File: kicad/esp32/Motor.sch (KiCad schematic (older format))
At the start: 4 parts, among them P2 Motor_L, P3 Motor_R, U4 DRV8835

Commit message: 自動配線成功
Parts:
- renumbered C15 to C10, P2 to P1, P3 to P2
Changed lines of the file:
@@
 $Descr A4 11693 8268
 encoding utf-8
-Sheet 2 13
+Sheet 2 14
 Title ""
 Date ""
@@
 	5600 3100 5600 3200
 $Comp
-L GND #PWR016
+L GND #PWR013
 U 1 1 57CA1E38
 P 5400 4200
-F 0 "#PWR016" H 5400 3950 50  0001 C CNN
+F 0 "#PWR013" H 5400 3950 50  0001 C CNN
 F 1 "GND" H 5400 4050 50  0000 C CNN
 F 2 "" H 5400 4200 50  0000 C CNN
@@
 	5400 4200 5400 4100
 $Comp
-L GND #PWR017
+L GND #PWR014
 U 1 1 57CA1E3F
 P 5700 4200
-F 0 "#PWR017" H 5700 3950 50  0001 C CNN
+F 0 "#PWR014" H 5700 3950 50  0001 C CNN
 F 1 "GND" H 5700 4050 50  0000 C CNN
 F 2 "" H 5700 4200 50  0000 C CNN
@@
 	5700 4200 5700 4100
 $Comp
-L GND #PWR018
+L GND #PWR015
 U 1 1 57CA1E46
 P 4800 4200
-F 0 "#PWR018" H 4800 3950 50  0001 C CNN
+F 0 "#PWR015" H 4800 3950 50  0001 C CNN
 F 1 "GND" H 4800 4050 50  0000 C CNN
 F 2 "" H 4800 4200 50  0000 C CNN
@@
 Motor
 $Comp
-L C C15
+L C C10
 U 1 1 57CCEFE0
 P 4000 3650
-F 0 "C15" H 4025 3750 50  0000 L CNN
+F 0 "C10" H 4025 3750 50  0000 L CNN
 F 1 "0.1u" H 4025 3550 50  0000 L CNN
 F 2 "Capacitors_SMD:C_0201" H 4038 3500 50  0001 C CNN
@@
 $EndComp
 $Comp
-L GND #PWR019
+L GND #PWR016
 U 1 1 57CCF046
 P 4000 4200
-F 0 "#PWR019" H 4000 3950 50  0001 C CNN
+F 0 "#PWR016" H 4000 3950 50  0001 C CNN
 F 1 "GND" H 4000 4050 50  0000 C CNN
 F 2 "" H 4000 4200 50  0000 C CNN
@@
 	4000 3800 4000 4200
 $Comp
-L +BATT #PWR020
+L +BATT #PWR017
 U 1 1 57CD5BEE
 P 5600 3100
-F 0 "#PWR020" H 5600 2950 50  0001 C CNN
+F 0 "#PWR017" H 5600 2950 50  0001 C CNN
 F 1 "+BATT" H 5600 3240 50  0000 C CNN
 F 2 "" H 5600 3100 50  0000 C CNN
@@
 	4900 3700 4800 3700
 $Comp
-L CONN_01X02 P2
+L CONN_01X02 P1
 U 1 1 589D679E
 P 7700 3450
-F 0 "P2" H 7700 3600 50  0000 C CNN
+F 0 "P1" H 7700 3600 50  0000 C CNN
 F 1 "Motor_L" V 7800 3450 50  0000 C CNN
 F 2 "mouse:SMD_conn_2" H 7700 3450 50  0001 C CNN
@@
 $EndComp
 $Comp
-L CONN_01X02 P3
+L CONN_01X02 P2
 U 1 1 589D680E
 P 7700 3950
-F 0 "P3" H 7700 4100 50  0000 C CNN
+F 0 "P2" H 7700 4100 50  0000 C CNN
 F 1 "Motor_R" V 7800 3950 50  0000 C CNN
 F 2 "mouse:SMD_conn_2" H 7700 3950 50  0001 C CNN
@@
 	7500 3500 7400 3500
 $Comp
-L +3.3V #PWR021
+L +3.3V #PWR018
 U 1 1 589CC6A5
 P 5300 3100
-F 0 "#PWR021" H 5300 2950 50  0001 C CNN
+F 0 "#PWR018" H 5300 2950 50  0001 C CNN
 F 1 "+3.3V" H 5300 3240 50  0000 C CNN
 F 2 "" H 5300 3100 50  0000 C CNN
@@
 $EndComp
 $Comp
-L +3.3V #PWR022
+L +3.3V #PWR019
 U 1 1 589CC6C6
 P 4000 3100
-F 0 "#PWR022" H 4000 2950 50  0001 C CNN
+F 0 "#PWR019" H 4000 2950 50  0001 C CNN
 F 1 "+3.3V" H 4000 3240 50  0000 C CNN
 F 2 "" H 4000 3100 50  0000 C CNN

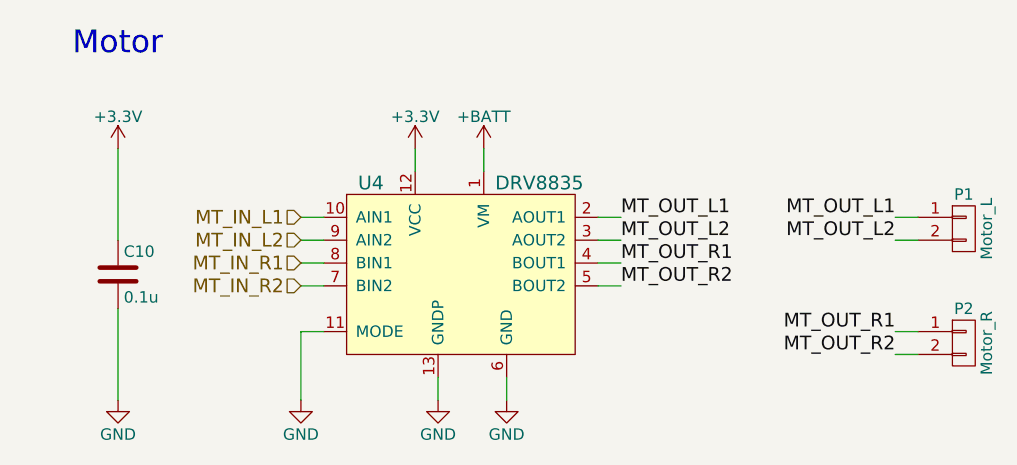
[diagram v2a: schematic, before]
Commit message: 2輪の基板を作成
部品を配置
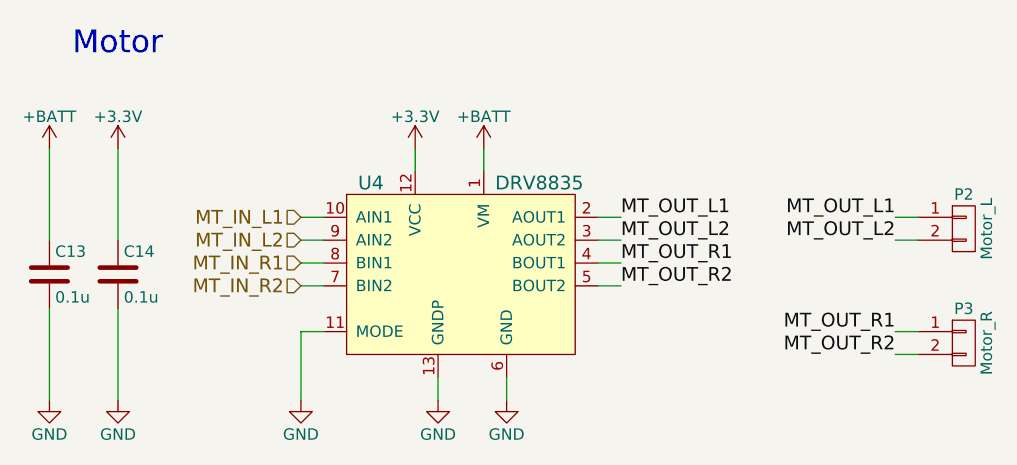
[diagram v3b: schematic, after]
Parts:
- added C13: 0.1u, Capacitors_SMD:C_0201, symbol C
- renumbered C10 to C14, P1 to P2, P2 to P3
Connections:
- net +BATT: now also C13.1
- net GND: now also C13.2
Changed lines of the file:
@@
 $Descr A4 11693 8268
 encoding utf-8
-Sheet 2 14
+Sheet 2 13
 Title ""
 Date ""
@@
 	5600 3100 5600 3200
 $Comp
-L GND #PWR013
+L GND #PWR014
 U 1 1 57CA1E38
 P 5400 4200
-F 0 "#PWR013" H 5400 3950 50  0001 C CNN
+F 0 "#PWR014" H 5400 3950 50  0001 C CNN
 F 1 "GND" H 5400 4050 50  0000 C CNN
 F 2 "" H 5400 4200 50  0000 C CNN
@@
 	5400 4200 5400 4100
 $Comp
-L GND #PWR014
+L GND #PWR015
 U 1 1 57CA1E3F
 P 5700 4200
-F 0 "#PWR014" H 5700 3950 50  0001 C CNN
+F 0 "#PWR015" H 5700 3950 50  0001 C CNN
 F 1 "GND" H 5700 4050 50  0000 C CNN
 F 2 "" H 5700 4200 50  0000 C CNN
@@
 	5700 4200 5700 4100
 $Comp
-L GND #PWR015
+L GND #PWR016
 U 1 1 57CA1E46
 P 4800 4200
-F 0 "#PWR015" H 4800 3950 50  0001 C CNN
+F 0 "#PWR016" H 4800 3950 50  0001 C CNN
 F 1 "GND" H 4800 4050 50  0000 C CNN
 F 2 "" H 4800 4200 50  0000 C CNN
@@
 Motor
 $Comp
-L C C10
+L C C14
 U 1 1 57CCEFE0
 P 4000 3650
-F 0 "C10" H 4025 3750 50  0000 L CNN
+F 0 "C14" H 4025 3750 50  0000 L CNN
 F 1 "0.1u" H 4025 3550 50  0000 L CNN
 F 2 "Capacitors_SMD:C_0201" H 4038 3500 50  0001 C CNN
@@
 $EndComp
 $Comp
-L GND #PWR016
+L GND #PWR017
 U 1 1 57CCF046
 P 4000 4200
-F 0 "#PWR016" H 4000 3950 50  0001 C CNN
+F 0 "#PWR017" H 4000 3950 50  0001 C CNN
 F 1 "GND" H 4000 4050 50  0000 C CNN
 F 2 "" H 4000 4200 50  0000 C CNN
@@
 	4000 3800 4000 4200
 $Comp
-L +BATT #PWR017
+L +BATT #PWR018
 U 1 1 57CD5BEE
 P 5600 3100
-F 0 "#PWR017" H 5600 2950 50  0001 C CNN
+F 0 "#PWR018" H 5600 2950 50  0001 C CNN
 F 1 "+BATT" H 5600 3240 50  0000 C CNN
 F 2 "" H 5600 3100 50  0000 C CNN
@@
 	4900 3700 4800 3700
 $Comp
-L CONN_01X02 P1
+L CONN_01X02 P2
 U 1 1 589D679E
 P 7700 3450
-F 0 "P1" H 7700 3600 50  0000 C CNN
+F 0 "P2" H 7700 3600 50  0000 C CNN
 F 1 "Motor_L" V 7800 3450 50  0000 C CNN
 F 2 "mouse:SMD_conn_2" H 7700 3450 50  0001 C CNN
@@
 $EndComp
 $Comp
-L CONN_01X02 P2
+L CONN_01X02 P3
 U 1 1 589D680E
 P 7700 3950
-F 0 "P2" H 7700 4100 50  0000 C CNN
+F 0 "P3" H 7700 4100 50  0000 C CNN
 F 1 "Motor_R" V 7800 3950 50  0000 C CNN
 F 2 "mouse:SMD_conn_2" H 7700 3950 50  0001 C CNN
@@
 	7500 3500 7400 3500
 $Comp
-L +3.3V #PWR018
+L +3.3V #PWR019
 U 1 1 589CC6A5
 P 5300 3100
-F 0 "#PWR018" H 5300 2950 50  0001 C CNN
+F 0 "#PWR019" H 5300 2950 50  0001 C CNN
 F 1 "+3.3V" H 5300 3240 50  0000 C CNN
 F 2 "" H 5300 3100 50  0000 C CNN
@@
 $EndComp
 $Comp
-L +3.3V #PWR019
+L +3.3V #PWR020
 U 1 1 589CC6C6
 P 4000 3100
-F 0 "#PWR019" H 4000 2950 50  0001 C CNN
+F 0 "#PWR020" H 4000 2950 50  0001 C CNN
 F 1 "+3.3V" H 4000 3240 50  0000 C CNN
 F 2 "" H 4000 3100 50  0000 C CNN
@@
 	1    0    0    -1
 $EndComp
+$Comp
+L +BATT #PWR021
+U 1 1 594721DF
+P 3700 3100
+F 0 "#PWR021" H 3700 2950 50  0001 C CNN
+F 1 "+BATT" H 3700 3240 50  0000 C CNN
+F 2 "" H 3700 3100 50  0000 C CNN
+F 3 "" H 3700 3100 50  0000 C CNN
+	1    3700 3100
+	1    0    0    -1
+$EndComp
+$Comp
+L C C13
+U 1 1 594721FA
+P 3700 3650
+F 0 "C13" H 3725 3750 50  0000 L CNN
+F 1 "0.1u" H 3725 3550 50  0000 L CNN
+F 2 "Capacitors_SMD:C_0201" H 3738 3500 50  0001 C CNN
+F 3 "" H 3700 3650 50  0000 C CNN
+	1    3700 3650
+	1    0    0    -1
+$EndComp
+$Comp
+L GND #PWR022
+U 1 1 59472221
+P 3700 4200
+F 0 "#PWR022" H 3700 3950 50  0001 C CNN
+F 1 "GND" H 3700 4050 50  0000 C CNN
+F 2 "" H 3700 4200 50  0000 C CNN
+F 3 "" H 3700 4200 50  0000 C CNN
+	1    3700 4200
+	1    0    0    -1
+$EndComp
+Wire Wire Line
+	3700 4200 3700 3800
+Wire Wire Line
+	3700 3500 3700 3100
 $EndSCHEMATC
